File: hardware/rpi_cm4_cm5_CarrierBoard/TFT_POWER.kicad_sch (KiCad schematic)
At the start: 86 parts, among them Q14 2N7002, Q15 2N7002, Q16 BCP56-16, Q17 ISP75DP06LMXTSA1, Q18 MMBT3904-7-F, U24 MAX16928CGUP, U25 TPS79901DRVR, U26 TPS61169DCKR, U27 AP22913W6-7

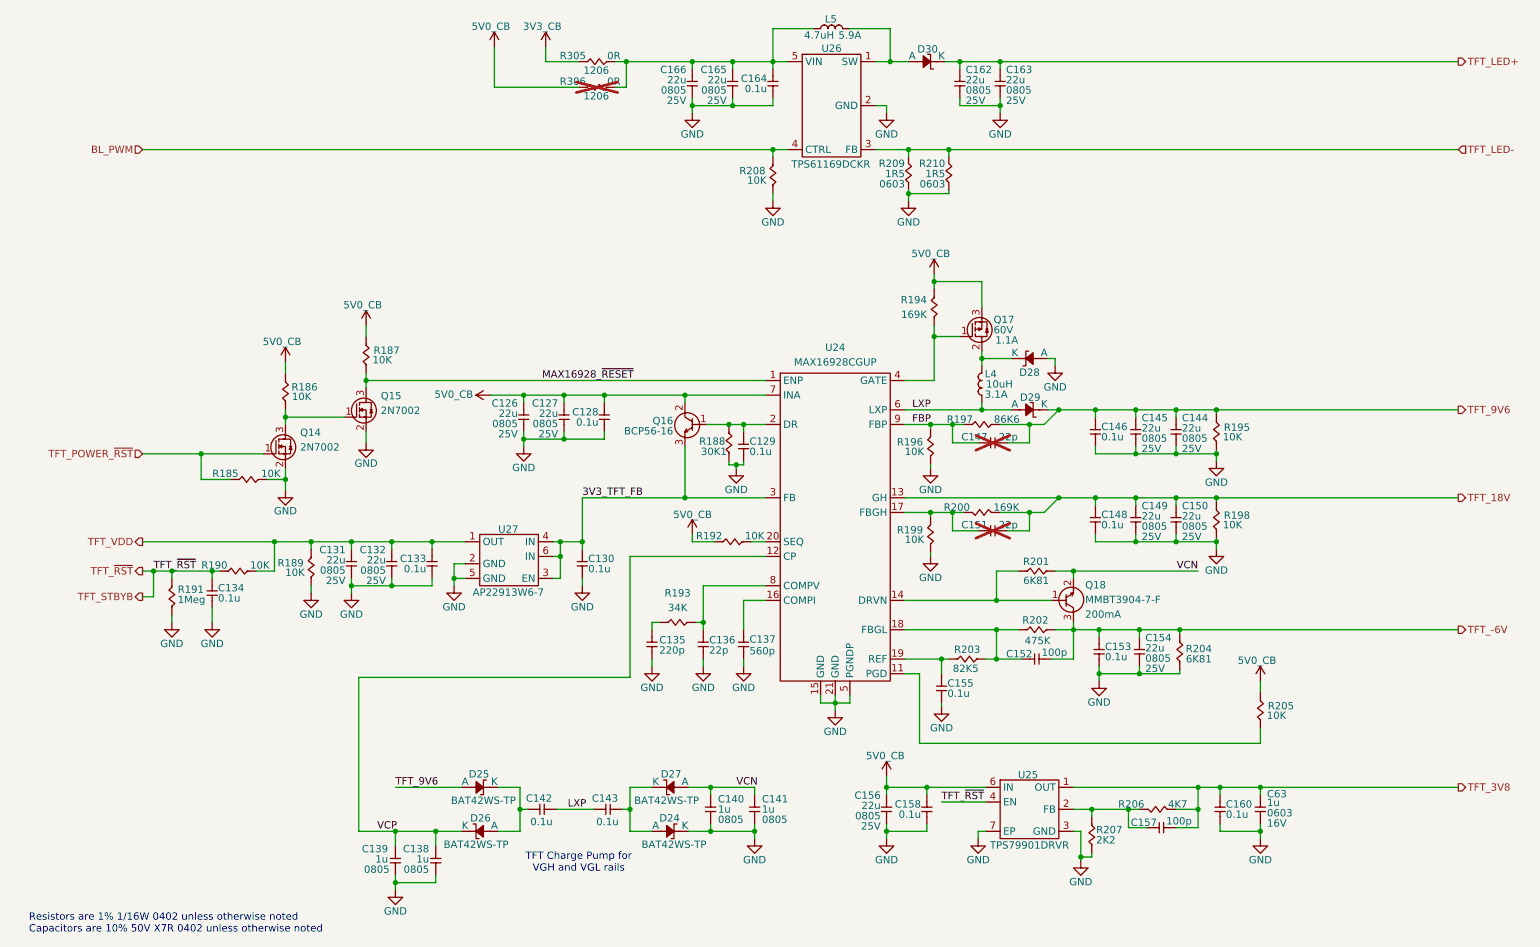
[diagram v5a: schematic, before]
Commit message: Document stackup Few changes to schematic based on preliminary PCB placement Update PinMux based on preliminary PCB placement and component positions
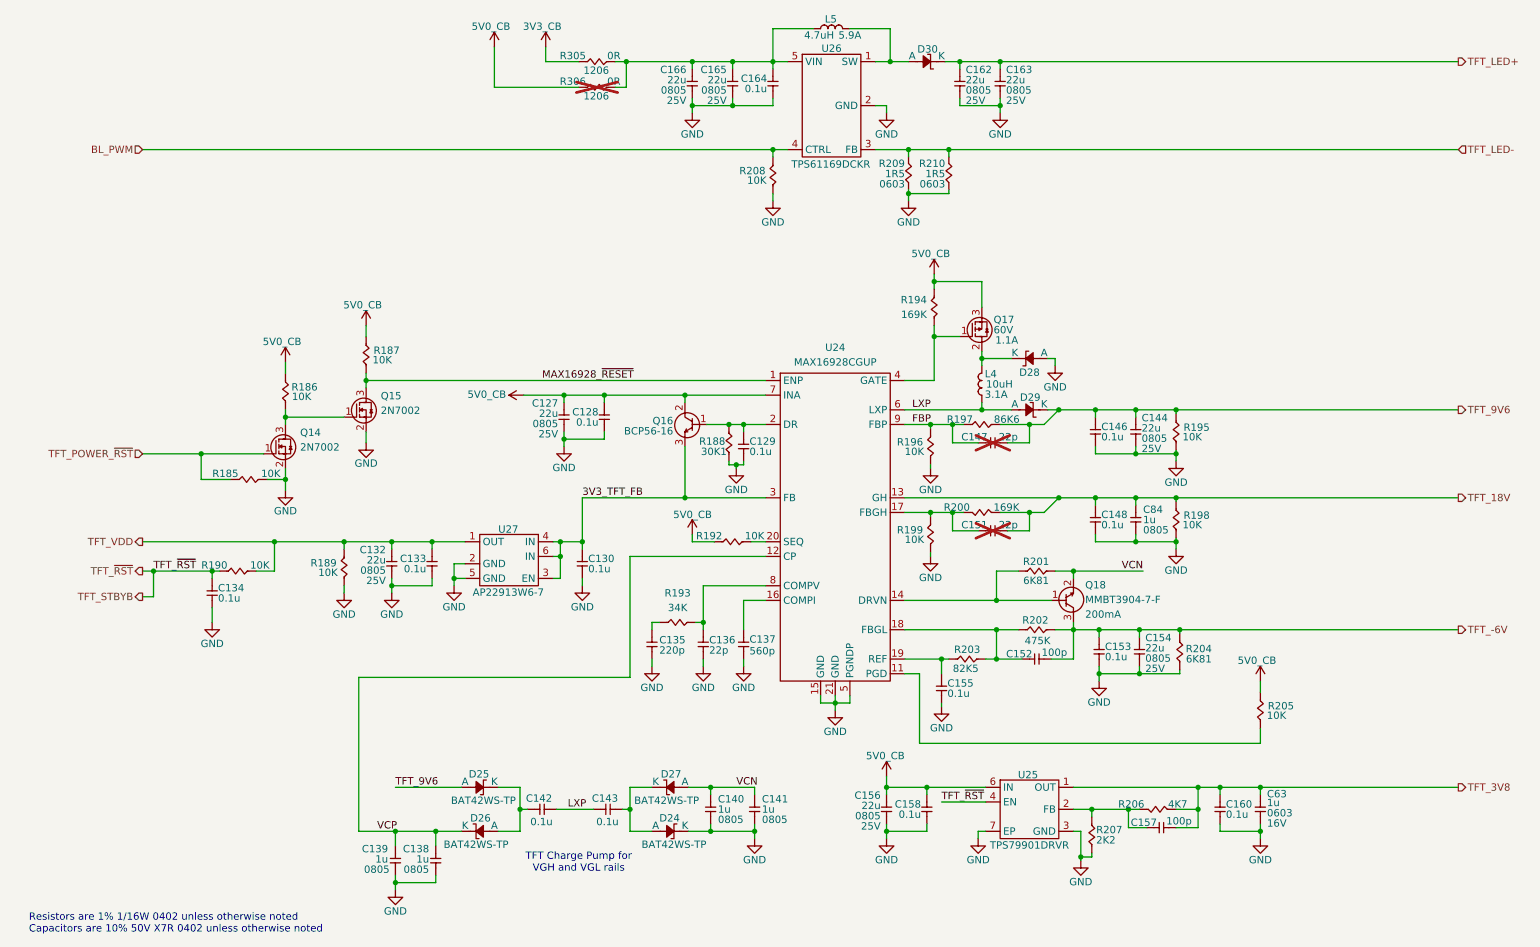
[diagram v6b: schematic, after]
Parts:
- removed C126, C131, C145, C149, C150: 22u, footprint:CAP_NONPOL_0805, symbol KicadCompDb:Capacitors/CAP_CER_SMT_00011
- removed R191: 1Meg, footprint:RES_0402, symbol KicadCompDb:Resistors/RES_SMT_00006
- added C84: 1u, footprint:CAP_NONPOL_0805, symbol KicadCompDb:Capacitors/CAP_CER_SMT_00002
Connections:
- net GND: now also C84.1
- net TFT_18V: now also C84.2
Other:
- moved on the sheet: C144, R189, R195, R198

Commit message: Continue working on the layout. Completed most of power planes planning and pouring Completed all DiffPairs routing and length matching (preliminary)
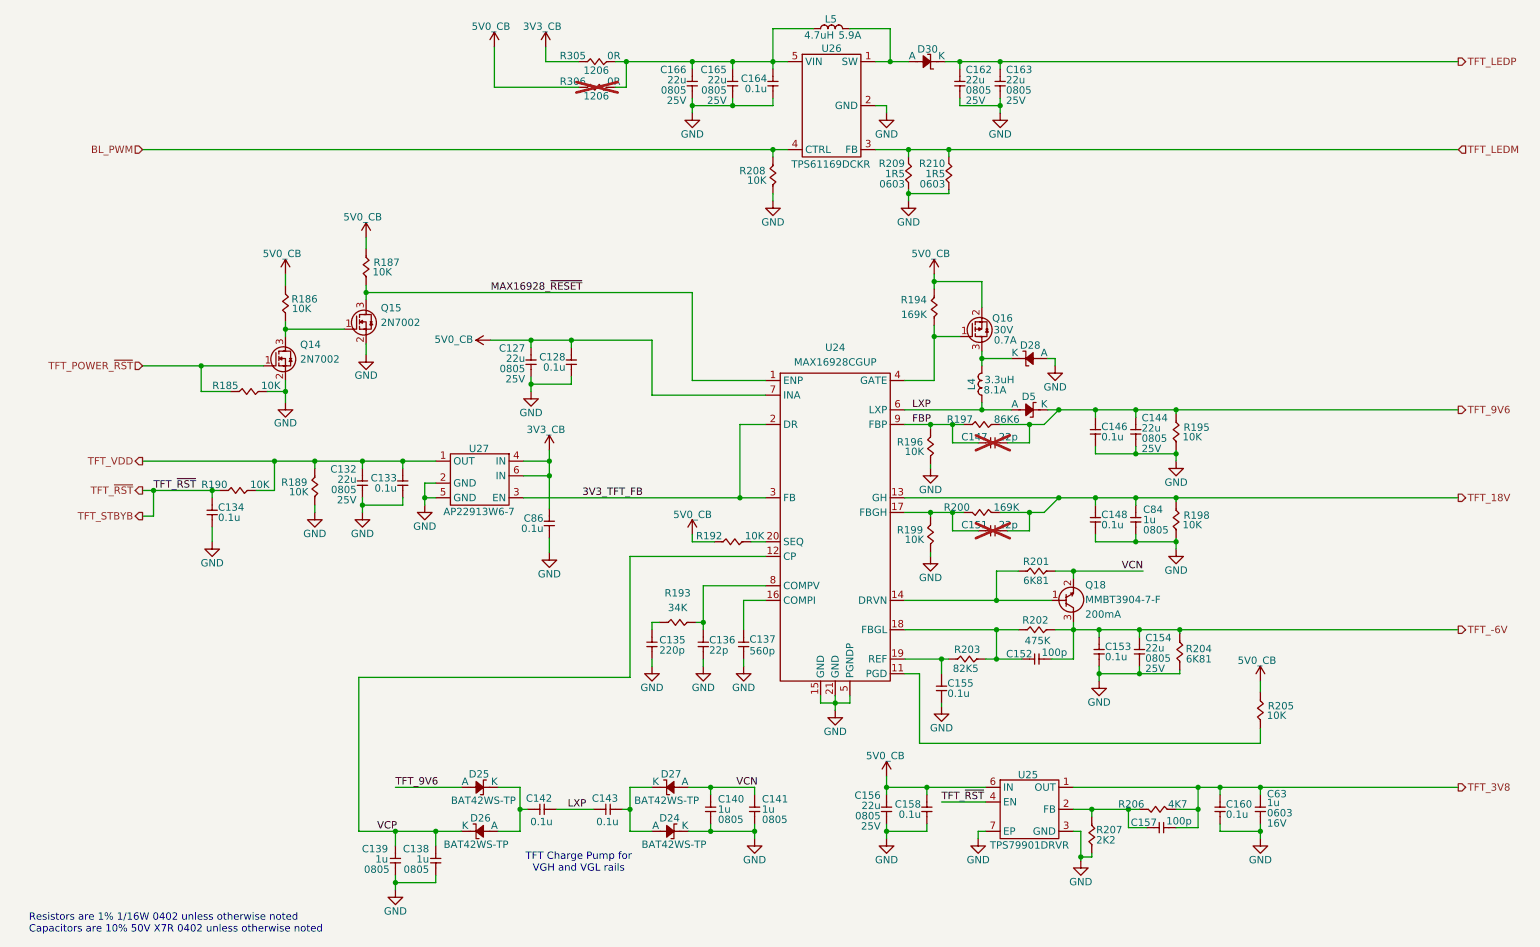
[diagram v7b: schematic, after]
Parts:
- removed C129, C130: 0.1u, footprint:CAP_NONPOL_0402, symbol KicadCompDb:Capacitors/CAP_CER_SMT_00001
- removed D28, D29: SK34A-LTP, footprint:DO-214AC, symbol KicadCompDb:Diodes/DIODE_00005
- removed L4: SRN8040-100M, footprint:SRN8040, symbol KicadCompDb:Inductor/IND_00004
- removed Q16: BCP56-16, footprint:SOT-223-4, symbol KicadCompDb:Bipolar/BIPOLAR_00002
- removed Q17: ISP75DP06LMXTSA1, footprint:SOT-223-4, symbol KicadCompDb:Mosfet/MOSFET_00004
- removed R188: 30K1, footprint:RES_0402, symbol KicadCompDb:Resistors/RES_SMT_00016
- added C86: 0.1u, footprint:CAP_NONPOL_0402, symbol KicadCompDb:Capacitors/CAP_CER_SMT_00001
- added D28, D5: BAT42WS-TP, footprint:SOD-323, symbol KicadCompDb:Diodes/DIODE_00006
- added L4: PA5003.332NLT, footprint:PA5003, symbol KicadCompDb:Inductor/IND_00006
- added Q16: DMP3030SN-7, footprint:SOT-23-3, symbol KicadCompDb:Mosfet/MOSFET_00006
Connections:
- net 3V3_CB: now also U27.4 (IN), U27.6 (IN), C86.2
- net 3V3_TFT_FB: now also U24.2 (DR); no longer U27.4 (IN), U27.6 (IN)
- net 5V0_CB: now also Q16.2 (S)
- net GND: now also C86.1, D28.2 (A)
- net LXP: now also D5.2 (A), L4.1
- net TFT_9V6: now also D5.1 (K)
- net at R194.1, U24.4 (GATE): now also Q16.1 (G)
- net TFT_LED+ renamed TFT_LEDP
- net TFT_LED- renamed TFT_LEDM
- new net: D28.1 (K), L4.2, Q16.3 (D)
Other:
- moved on the sheet: C127, C128, C132, C133, C134, Q14, Q15, R185, R186, R187, R189, R190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

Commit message: Significant update Stackup changed from 6 to 8 layers Changed design notes accordingly Re-routed all differential pairs and length match / skew match Fanout critical signals away from dense areas 95% routing completed
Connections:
- net VCN renamed VCneg
- net VCP renamed VCpos
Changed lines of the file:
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@@
 	(title_block
 		(title "RPI CMx Carrier")
-		(date "2026-01-22")
+		(date "2026-02-13")
 		(rev "2.00-0A")
 		(comment 1 "Jean-Francois Bilodeau")
@@
 		)
 	)
-	(label "VCP"
+	(label "VCpos"
 		(at 73.025 154.94 0)
 		(effects
@@
 		)
 	)
-	(label "VCN"
+	(label "VCneg"
 		(at 205.74 109.855 180)
 		(effects
@@
 		)
 	)
-	(label "VCN"
+	(label "VCneg"
 		(at 135.255 147.32 0)
 		(effects
